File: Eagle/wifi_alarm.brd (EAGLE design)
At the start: 60.6 x 74.9 mm, 15 parts, among them T1 BC547

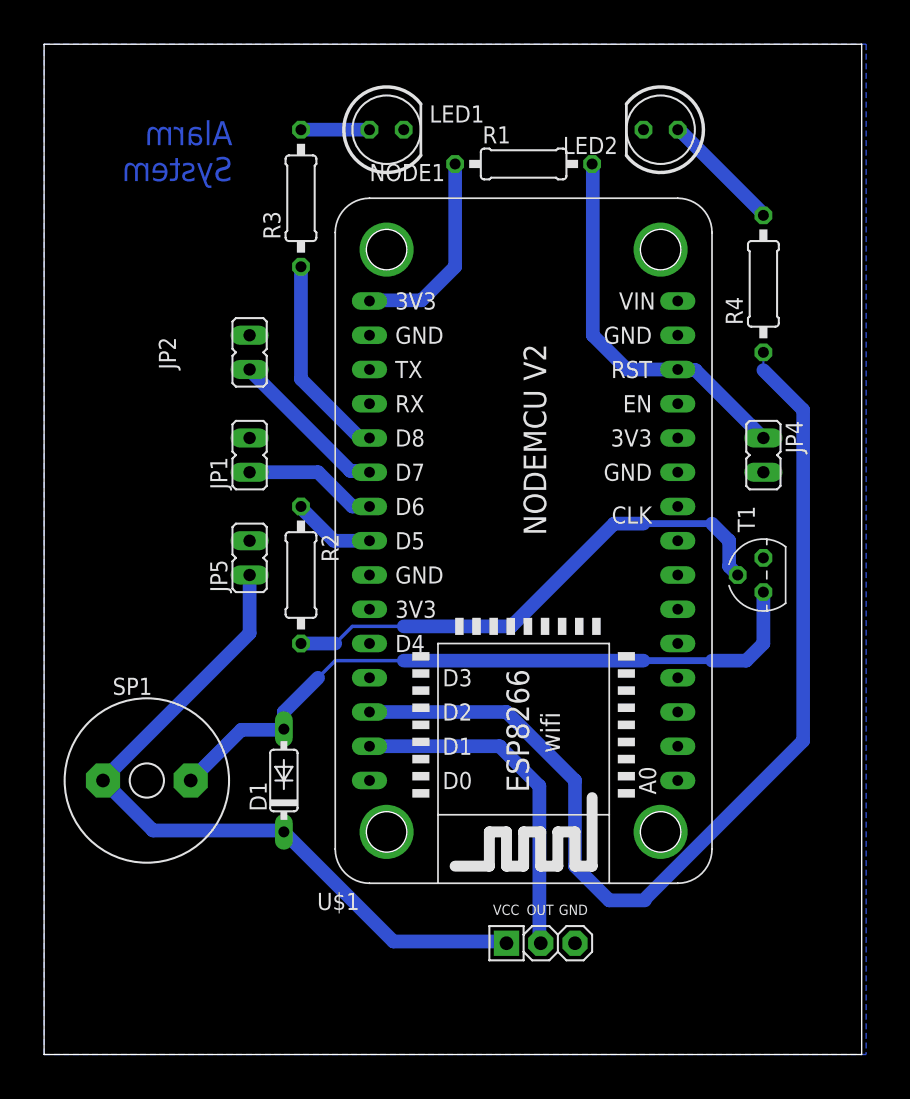
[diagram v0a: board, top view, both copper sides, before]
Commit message: Changed names, values and rearranged Eagle schematics
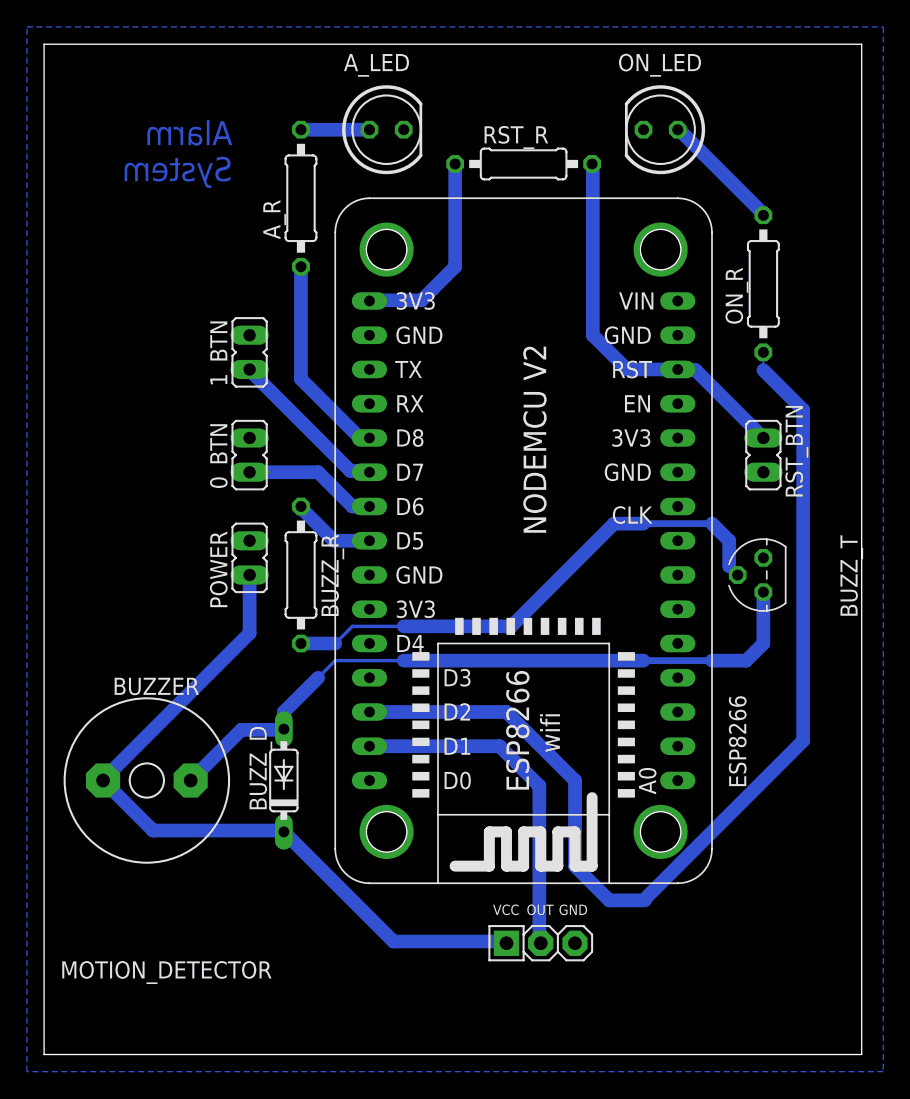
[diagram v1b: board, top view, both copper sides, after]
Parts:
- A_R: value (none) -> 22
- BUZZ_D: value 1N4148DO35-7 -> 1N4148
- BUZZ_R: value (none) -> 1k
- ON_R: value (none) -> 100
- RST_R: value (none) -> 10k
- renumbered D1 to BUZZ_D, JP1 to 0_BTN, JP2 to 1_BTN, JP4 to RST_BTN, JP5 to POWER, LED1 to A_LED, LED2 to ON_LED, NODE1 to ESP8266, R1 to RST_R, R2 to BUZZ_R, R3 to A_R, R4 to ON_R, SP1 to BUZZER, T1 to BUZZ_T, U$1 to MOTION_DETECTOR
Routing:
- net N$8: track 38.8 -> 37.9 mm
